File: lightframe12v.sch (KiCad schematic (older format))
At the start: 46 parts, among them J1 PJ-077, J2 Conn_01x06_Female, J3 Conn_01x06_Female, J4 Conn_01x06_Female, J5 Conn_01x10_Female, Q1 MMBT2222, Q2 MMBT2222, SW1 SW_Push, SW2 SW_Push, U1 ESP32-WROOM-32U, U2 TPS563207s, U3 TLC5971

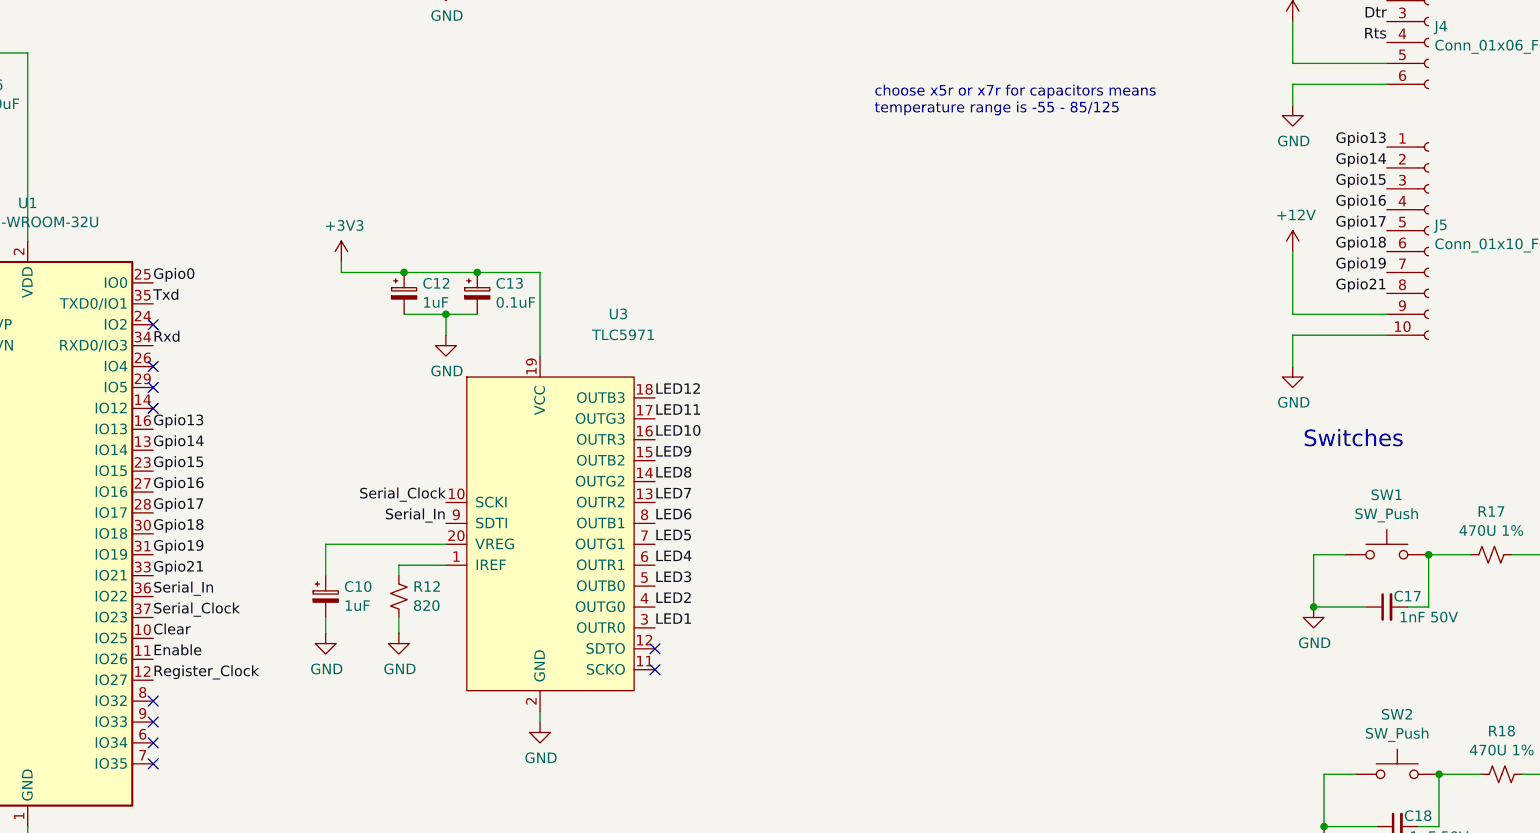
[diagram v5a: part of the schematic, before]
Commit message: improves wroom layout
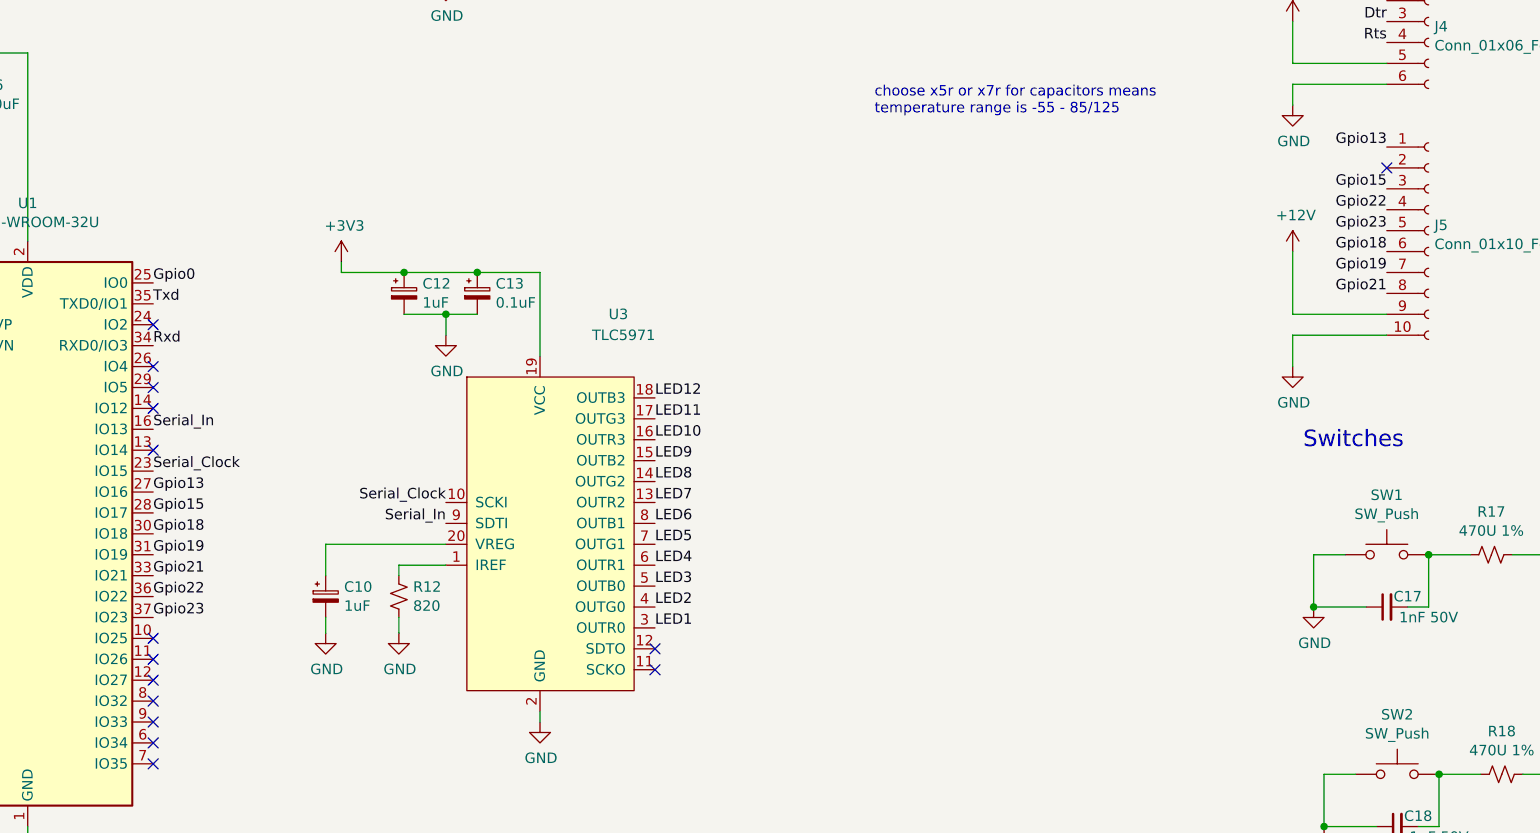
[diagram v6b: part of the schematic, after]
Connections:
- net Gpio13: now also U1.27 (IO16); no longer U1.16 (IO13)
- net Gpio15: now also U1.28 (IO17); no longer U1.23 (IO15)
- net Serial_Clock: now also U1.23 (IO15); no longer U1.37 (IO23)
- net Serial_In: now also U1.16 (IO13); no longer U1.36 (IO22)
- net Clear: no longer names the net of U1.10 (IO25)
- net Enable: no longer names the net of U1.11 (IO26)
- net Gpio14: no longer names the net of J5.2 (Pin_2)
- net Gpio14: no longer U1.13 (IO14)
- net Gpio16 renamed Gpio22
- net Gpio22: now also U1.36 (IO22); no longer U1.27 (IO16)
- net Gpio17 renamed Gpio23
- net Gpio23: now also U1.37 (IO23); no longer U1.28 (IO17)
- net Register_Clock: no longer names the net of U1.12 (IO27)
- no-connect marks 18 -> 23
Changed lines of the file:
@@
 SPMWH22286D5WAP0S2/7347178\nVf=3.1V, I=60mA
 Text Label 10100 3150 2    50   ~ 0
-Gpio16
+Gpio22
 Text Label 10100 3050 2    50   ~ 0
 Gpio15
-Text Label 10100 2950 2    50   ~ 0
-Gpio14
 Text Label 10100 2850 2    50   ~ 0
 Gpio13
@@
 Gpio18
 Text Label 10100 3250 2    50   ~ 0
-Gpio17
+Gpio23
 $Comp
 L Connector:Conn_01x10_Female J5
@@
 Text Label 4200 4700 0    50   ~ 0
 Gpio18
+Text Label 4200 5100 0    50   ~ 0
+Gpio23
+Text Label 4200 5000 0    50   ~ 0
+Gpio22
 Text Label 4200 4600 0    50   ~ 0
-Gpio17
+Gpio15
 Text Label 4200 4500 0    50   ~ 0
-Gpio16
-Text Label 4200 4400 0    50   ~ 0
-Gpio15
-Text Label 4200 4300 0    50   ~ 0
-Gpio14
+Gpio13
 Text Label 4200 4200 0    50   ~ 0
-Gpio13
-Text Label 4200 5000 0    50   ~ 0
 Serial_In
-Text Label 4200 5200 0    50   ~ 0
-Clear
-Text Label 4200 5300 0    50   ~ 0
-Enable
 NoConn ~ 4200 5500
 NoConn ~ 4200 5600
@@
 Wire Wire Line
 	6050 5550 6050 5600
-Text Label 4200 5400 0    50   ~ 0
-Register_Clock
-Text Label 4200 5100 0    50   ~ 0
+Text Label 4200 4400 0    50   ~ 0
 Serial_Clock
 $Comp
@@
 Wire Wire Line
 	2850 2900 3300 2900
+NoConn ~ 4200 5200
+NoConn ~ 4200 5300
+NoConn ~ 4200 5400
+NoConn ~ 4200 4300
+NoConn ~ 10100 2950
 $EndSCHEMATC

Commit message: Rearranges around power  traces.
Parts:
- J4: value Conn_01x06_Female -> Conn_01x04_Female; footprint Connector_PinHeader_2.54mm:PinHeader_1x06_P2.54mm_Vertical -> Connector_PinSocket_2.54mm:PinSocket_1x04_P2.54mm_Vertical; symbol Connector:Conn_01x06_Female -> Connector:Conn_01x04_Female
- J5: value Conn_01x10_Female -> Conn_01x5_Female; footprint Connector_PinHeader_2.54mm:PinHeader_1x10_P2.54mm_Vertical -> Connector_PinSocket_2.54mm:PinSocket_1x05_P2.54mm_Vertical; symbol Connector:Conn_01x10_Female -> Connector:Conn_01x05_Female
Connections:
- net +12V: no longer J5.9 (Pin_9)
- net +3V3: no longer J4.5 (Pin_5)
- net GND: no longer J4.6 (Pin_6), J5.10 (Pin_10)
- net Gpio15: now also J5.2 (Pin_2); no longer J5.3 (Pin_3)
- net Gpio18: now also J5.3 (Pin_3); no longer J5.6 (Pin_6)
- net Gpio19: now also J5.4 (Pin_4); no longer J5.7 (Pin_7)
- net Gpio21: now also J5.5 (Pin_5); no longer J5.8 (Pin_8)
- net Gpio22: no longer J5.4 (Pin_4)
- net Gpio23: no longer J5.5 (Pin_5)
- net Rxd: now also J4.1 (Pin_1); no longer J4.2 (Pin_2)
- net Txd: now also J4.2 (Pin_2); no longer J4.1 (Pin_1)
- no-connect marks 23 -> 22
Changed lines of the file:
@@
 	0    -1   -1   0
 $EndComp
-$Comp
-L power:+3V3 #PWR020
-U 1 1 60361EF1
-P 9650 2250
-F 0 "#PWR020" H 9650 2100 50  0001 C CNN
-F 1 "+3V3" H 9665 2423 50  0000 C CNN
-F 2 "" H 9650 2250 50  0001 C CNN
-F 3 "" H 9650 2250 50  0001 C CNN
-	1    9650 2250
-	1    0    0    -1
-$EndComp
-$Comp
-L power:GND #PWR021
-U 1 1 60361772
-P 9650 2650
-F 0 "#PWR021" H 9650 2400 50  0001 C CNN
-F 1 "GND" H 9655 2477 50  0000 C CNN
-F 2 "" H 9650 2650 50  0001 C CNN
-F 3 "" H 9650 2650 50  0001 C CNN
-	1    9650 2650
-	1    0    0    -1
-$EndComp
-Wire Wire Line
-	9650 2550 9650 2650
-Wire Wire Line
-	10100 2550 9650 2550
-Wire Wire Line
-	9650 2450 9650 2250
-Wire Wire Line
-	10100 2450 9650 2450
 Text Notes 9700 700  0    79   ~ 0
 Connections
-Text Label 10100 2250 2    50   ~ 0
+Text Label 10100 2350 2    50   ~ 0
 Dtr
-Text Label 10100 2350 2    50   ~ 0
+Text Label 10100 2450 2    50   ~ 0
 Rts
 Text Notes 11150 1050 2    50   ~ 0
 SPMWH22286D5WAP0S2/7347178\nVf=3.1V, I=60mA
 Text Label 10100 3150 2    50   ~ 0
-Gpio22
+Gpio15
 Text Label 10100 3050 2    50   ~ 0
-Gpio15
-Text Label 10100 2850 2    50   ~ 0
 Gpio13
 Text Label 10100 2150 2    50   ~ 0
 Rxd
-Text Label 10100 2050 2    50   ~ 0
+Text Label 10100 2250 2    50   ~ 0
 Txd
 $Comp
-L Connector:Conn_01x06_Female J4
+L Connector:Conn_01x04_Female J4
 U 1 1 600DF393
 P 10300 2250
 F 0 "J4" H 10328 2226 50  0000 L CNN
-F 1 "Conn_01x06_Female" H 10328 2135 50  0000 L CNN
-F 2 "Connector_PinHeader_2.54mm:PinHeader_1x06_P2.54mm_Vertical" H 10300 2250 50  0001 C CNN
+F 1 "Conn_01x04_Female" H 10328 2135 50  0000 L CNN
+F 2 "Connector_PinSocket_2.54mm:PinSocket_1x04_P2.54mm_Vertical" H 10300 2250 50  0001 C CNN
 F 3 "~" H 10300 2250 50  0001 C CNN
 	1    10300 2250
-	1    0    0    -1
-$EndComp
-$Comp
-L power:+12V #PWR022
-U 1 1 605170D9
-P 9650 3350
-F 0 "#PWR022" H 9650 3200 50  0001 C CNN
-F 1 "+12V" H 9665 3523 50  0000 C CNN
-F 2 "" H 9650 3350 50  0001 C CNN
-F 3 "" H 9650 3350 50  0001 C CNN
-	1    9650 3350
 	1    0    0    -1
 $EndComp
@@
 	0    -1   -1   0
 $EndComp
-Wire Wire Line
-	9650 3650 9650 3350
-Wire Wire Line
-	10100 3650 9650 3650
-Wire Wire Line
-	9650 3750 9650 3900
-Wire Wire Line
-	10100 3750 9650 3750
-$Comp
-L power:GND #PWR023
-U 1 1 602BC193
-P 9650 3900
-F 0 "#PWR023" H 9650 3650 50  0001 C CNN
-F 1 "GND" H 9655 3727 50  0000 C CNN
-F 2 "" H 9650 3900 50  0001 C CNN
-F 3 "" H 9650 3900 50  0001 C CNN
-	1    9650 3900
-	1    0    0    -1
-$EndComp
-Text Label 10100 3550 2    50   ~ 0
+Text Label 10100 3450 2    50   ~ 0
 Gpio21
-Text Label 10100 3450 2    50   ~ 0
+Text Label 10100 3350 2    50   ~ 0
 Gpio19
-Text Label 10100 3350 2    50   ~ 0
+Text Label 10100 3250 2    50   ~ 0
 Gpio18
-Text Label 10100 3250 2    50   ~ 0
-Gpio23
-$Comp
-L Connector:Conn_01x10_Female J5
+$Comp
+L Connector:Conn_01x05_Female J5
 U 1 1 601E8B71
 P 10300 3250
 F 0 "J5" H 10328 3276 50  0000 L CNN
-F 1 "Conn_01x10_Female" H 10328 3185 50  0000 L CNN
-F 2 "Connector_PinHeader_2.54mm:PinHeader_1x10_P2.54mm_Vertical" H 10300 3250 50  0001 C CNN
+F 1 "Conn_01x5_Female" H 10328 3185 50  0000 L CNN
+F 2 "Connector_PinSocket_2.54mm:PinSocket_1x05_P2.54mm_Vertical" H 10300 3250 50  0001 C CNN
 F 3 "~" H 10300 3250 50  0001 C CNN
 	1    10300 3250
@@
 NoConn ~ 4200 5400
 NoConn ~ 4200 4300
-NoConn ~ 10100 2950
 $EndSCHEMATC

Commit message: Moves led driver
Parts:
- J5: value Conn_01x5_Female -> Conn_01x6_Female; footprint Connector_PinSocket_2.54mm:PinSocket_1x05_P2.54mm_Vertical -> Connector_PinSocket_2.54mm:PinSocket_1x06_P2.54mm_Vertical; symbol Connector:Conn_01x05_Female -> Connector:Conn_01x06_Female
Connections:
- net Serial_Clock: now also U1.26 (IO4); no longer U1.23 (IO15)
- net Serial_In: now also U1.27 (IO16); no longer U1.16 (IO13)
- net Gpio26: now reaches U1.11 (IO26)
- net Gpio26: now also J5.2 (Pin_2)
- net Gpio27: now reaches U1.12 (IO27)
- net Gpio27: now also J5.1 (Pin_1)
- net Gpio34: now reaches U1.6 (IO34)
- net Gpio34: now also J5.6 (Pin_6)
- net Gpio35: now reaches U1.7 (IO35)
- net Gpio35: now also J5.5 (Pin_5)
- net Gpio32: now reaches U1.8 (IO32)
- net Gpio32: now also J5.4 (Pin_4)
- net Gpio33: now reaches U1.9 (IO33)
- net Gpio33: now also J5.3 (Pin_3)
- removed net Gpio13: J5.1 (Pin_1), U1.27 (IO16)
- net Gpio15: no longer names the net of U1.28 (IO17)
- net Gpio15: no longer J5.2 (Pin_2)
- net Gpio18: no longer names the net of U1.30 (IO18)
- net Gpio18: no longer J5.3 (Pin_3)
- net Gpio19: no longer names the net of U1.31 (IO19)
- net Gpio19: no longer J5.4 (Pin_4)
- net Gpio21: no longer names the net of U1.33 (IO21)
- net Gpio21: no longer J5.5 (Pin_5)
- net Gpio22: no longer names the net of U1.36 (IO22)
- net Gpio23: no longer names the net of U1.37 (IO23)
- no-connect marks 22 -> 24
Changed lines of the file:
@@
 Text Notes 11150 1050 2    50   ~ 0
 SPMWH22286D5WAP0S2/7347178\nVf=3.1V, I=60mA
-Text Label 10100 3150 2    50   ~ 0
-Gpio15
-Text Label 10100 3050 2    50   ~ 0
-Gpio13
 Text Label 10100 2150 2    50   ~ 0
 Rxd
@@
 	0    -1   -1   0
 $EndComp
-Text Label 10100 3450 2    50   ~ 0
-Gpio21
-Text Label 10100 3350 2    50   ~ 0
-Gpio19
-Text Label 10100 3250 2    50   ~ 0
-Gpio18
-$Comp
-L Connector:Conn_01x05_Female J5
+$Comp
+L Connector:Conn_01x06_Female J5
 U 1 1 601E8B71
 P 10300 3250
 F 0 "J5" H 10328 3276 50  0000 L CNN
-F 1 "Conn_01x5_Female" H 10328 3185 50  0000 L CNN
-F 2 "Connector_PinSocket_2.54mm:PinSocket_1x05_P2.54mm_Vertical" H 10300 3250 50  0001 C CNN
+F 1 "Conn_01x6_Female" H 10328 3185 50  0000 L CNN
+F 2 "Connector_PinSocket_2.54mm:PinSocket_1x06_P2.54mm_Vertical" H 10300 3250 50  0001 C CNN
 F 3 "~" H 10300 3250 50  0001 C CNN
 	1    10300 3250
@@
 Wire Wire Line
 	2450 2900 2500 2900
-$Comp
-L RF_Module:ESP32-WROOM-32U U1
-U 1 1 60541BAF
-P 3600 4700
-F 0 "U1" H 3600 6281 50  0000 C CNN
-F 1 "ESP32-WROOM-32U" H 3600 6190 50  0000 C CNN
-F 2 "RF_Module:ESP32-WROOM-32U" H 3600 3200 50  0001 C CNN
-F 3 "https://www.espressif.com/sites/default/files/documentation/esp32-wroom-32d_esp32-wroom-32u_datasheet_en.pdf" H 3300 4750 50  0001 C CNN
-	1    3600 4700
-	1    0    0    -1
-$EndComp
 Text Label 3000 3500 2    50   ~ 0
 Reset
@@
 Txd
 NoConn ~ 4200 3700
-NoConn ~ 4200 3900
 NoConn ~ 4200 4000
 NoConn ~ 4200 4100
-Text Label 4200 4900 0    50   ~ 0
-Gpio21
-Text Label 4200 4800 0    50   ~ 0
-Gpio19
-Text Label 4200 4700 0    50   ~ 0
-Gpio18
-Text Label 4200 5100 0    50   ~ 0
-Gpio23
-Text Label 4200 5000 0    50   ~ 0
-Gpio22
-Text Label 4200 4600 0    50   ~ 0
-Gpio15
 Text Label 4200 4500 0    50   ~ 0
-Gpio13
-Text Label 4200 4200 0    50   ~ 0
 Serial_In
-NoConn ~ 4200 5500
-NoConn ~ 4200 5600
-NoConn ~ 4200 5700
-NoConn ~ 4200 5800
 Wire Wire Line
 	3600 6100 3600 6150
@@
 Wire Wire Line
 	6050 5550 6050 5600
-Text Label 4200 4400 0    50   ~ 0
+Text Label 4200 3900 0    50   ~ 0
 Serial_Clock
 $Comp
@@
 Wire Wire Line
 	2850 2900 3300 2900
+NoConn ~ 4200 4300
+$Comp
+L RF_Module:ESP32-WROOM-32U U1
+U 1 1 60541BAF
+P 3600 4700
+F 0 "U1" H 3600 6281 50  0000 C CNN
+F 1 "ESP32-WROOM-32U" H 3600 6190 50  0000 C CNN
+F 2 "RF_Module:ESP32-WROOM-32U" H 3600 3200 50  0001 C CNN
+F 3 "https://www.espressif.com/sites/default/files/documentation/esp32-wroom-32d_esp32-wroom-32u_datasheet_en.pdf" H 3300 4750 50  0001 C CNN
+	1    3600 4700
+	1    0    0    -1
+$EndComp
+NoConn ~ 4200 4400
+NoConn ~ 4200 4200
+Text Label 4200 5700 0    50   ~ 0
+Gpio34
+Text Label 4200 5800 0    50   ~ 0
+Gpio35
+Text Label 4200 5400 0    50   ~ 0
+Gpio27
+Text Label 4200 5500 0    50   ~ 0
+Gpio32
+Text Label 4200 5600 0    50   ~ 0
+Gpio33
+Text Label 4200 5300 0    50   ~ 0
+Gpio26
+Text Label 10100 3550 2    50   ~ 0
+Gpio34
+Text Label 10100 3450 2    50   ~ 0
+Gpio35
+Text Label 10100 3050 2    50   ~ 0
+Gpio27
+Text Label 10100 3350 2    50   ~ 0
+Gpio32
+Text Label 10100 3250 2    50   ~ 0
+Gpio33
+Text Label 10100 3150 2    50   ~ 0
+Gpio26
+NoConn ~ 4200 4600
+NoConn ~ 4200 4700
+NoConn ~ 4200 4800
+NoConn ~ 4200 4900
+NoConn ~ 4200 5000
+NoConn ~ 4200 5100
 NoConn ~ 4200 5200
-NoConn ~ 4200 5300
-NoConn ~ 4200 5400
-NoConn ~ 4200 4300
+NoConn ~ 10175 575
 $EndSCHEMATC
